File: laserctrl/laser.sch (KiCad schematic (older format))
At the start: 23 parts

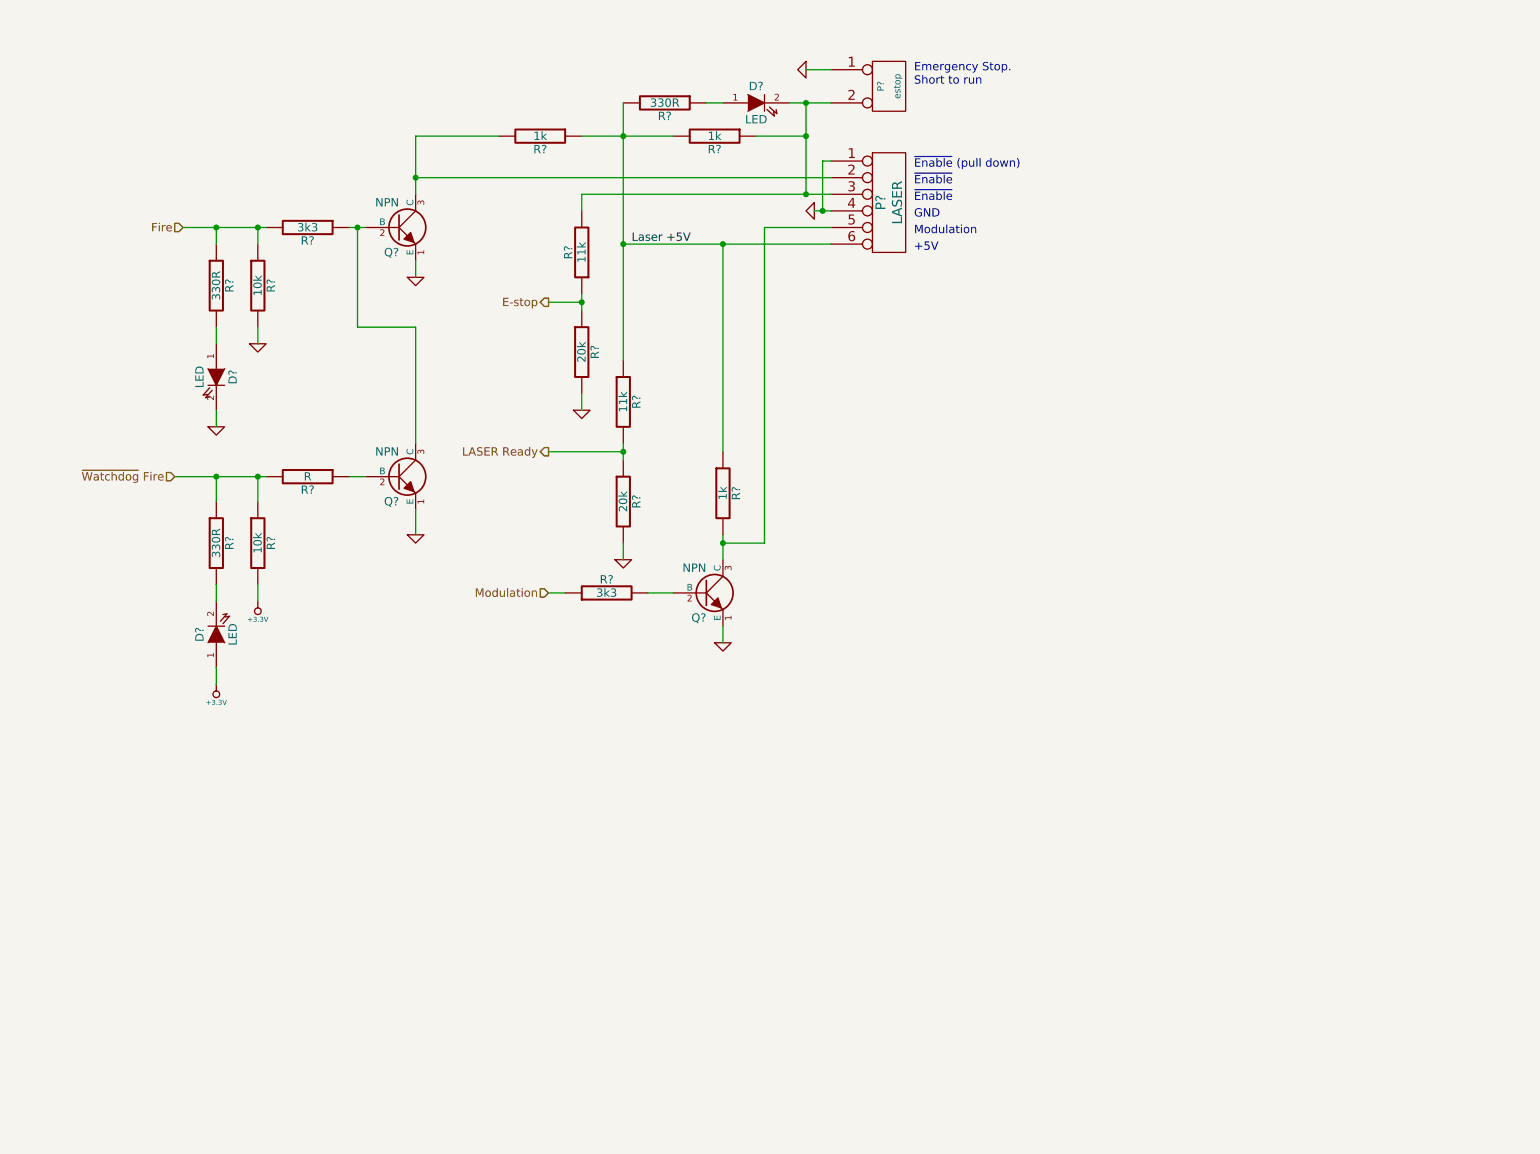
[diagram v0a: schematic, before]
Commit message: Added optocouplers to the LASER interface to protect against induced transients
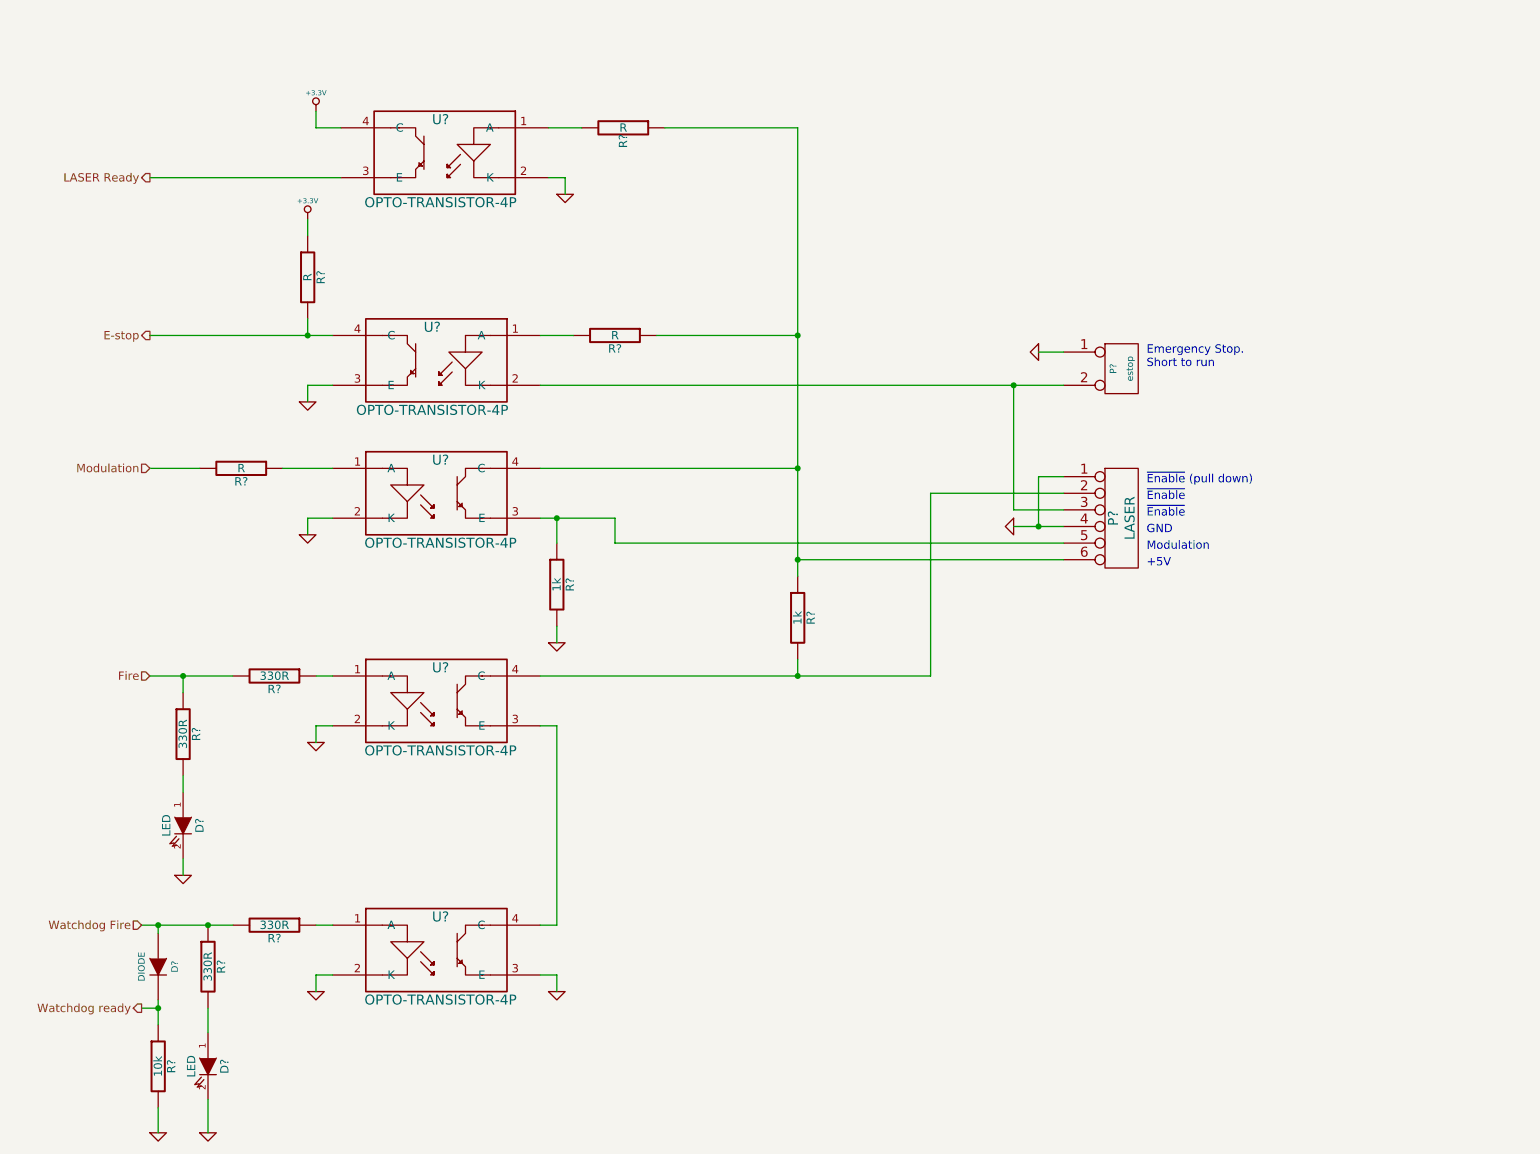
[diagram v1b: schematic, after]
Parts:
- removed D?: LED, symbol LED
- removed Q? (x3): NPN, symbol NPN
- removed R? (x3): 1k, symbol R
- removed R?: 3k3, symbol R
- removed R?: 330R, symbol R
- removed R? (x2): 11k, symbol R
- removed R? (x2): 20k, symbol R
- removed R? (x2): 10k, symbol R
- added D?: DIODE, symbol DIODE
- added R? (x4): R, symbol R
- added R? (x2): 1k, symbol R
- added R?: 10k, symbol R
- added U? (x5): OPTO-TRANSISTOR-4P, symbol OPTO-TRANSISTOR-4P
- R?: value 3k3 -> 330R
- R?: value R -> 330R
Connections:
- net +3.3V: now also R?.1, U?.4 (C); no longer D?.1 (A)
- net E-stop: now also R?.2, U?.4 (C)
- net GND: now also D?.2 (K), R?.2, R?.2, U?.2 (K), U?.2 (K), U?.2 (K), U?.2 (K), U?.3 (E), U?.3 (E)
- net LASER Ready: now also U?.3 (E)
- net Modulation: now also R?.2
- net at P?.2: now also R?.2, U?.4 (C)
- net at P?.2 (PM), P?.3: now also U?.2 (K)
- net at P?.5: now also R?.1, U?.3 (E)
- net at R?.1: now also U?.1 (A) (x2)
- net at R?.2: now also D?.1 (A); no longer D?.2 (K)
- net Laser +5V: no longer names the net of P?.6
- net Laser +5V: now also R?.1, R?.1, R?.1, U?.4 (C)
- net ~Watchdog Fire renamed Watchdog Fire
- net Watchdog Fire: now also D?.1 (A)
- new net: U?.3 (E), U?.4 (C)
- new net: R?.2, U?.1 (A) (x2)
- new net: R?.1, U?.1 (A)
- new net Watchdog ready: D?.2 (K), R?.1
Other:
- moved on the sheet: D?, P?, R?

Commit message: Added transistors to drive the optocouplers
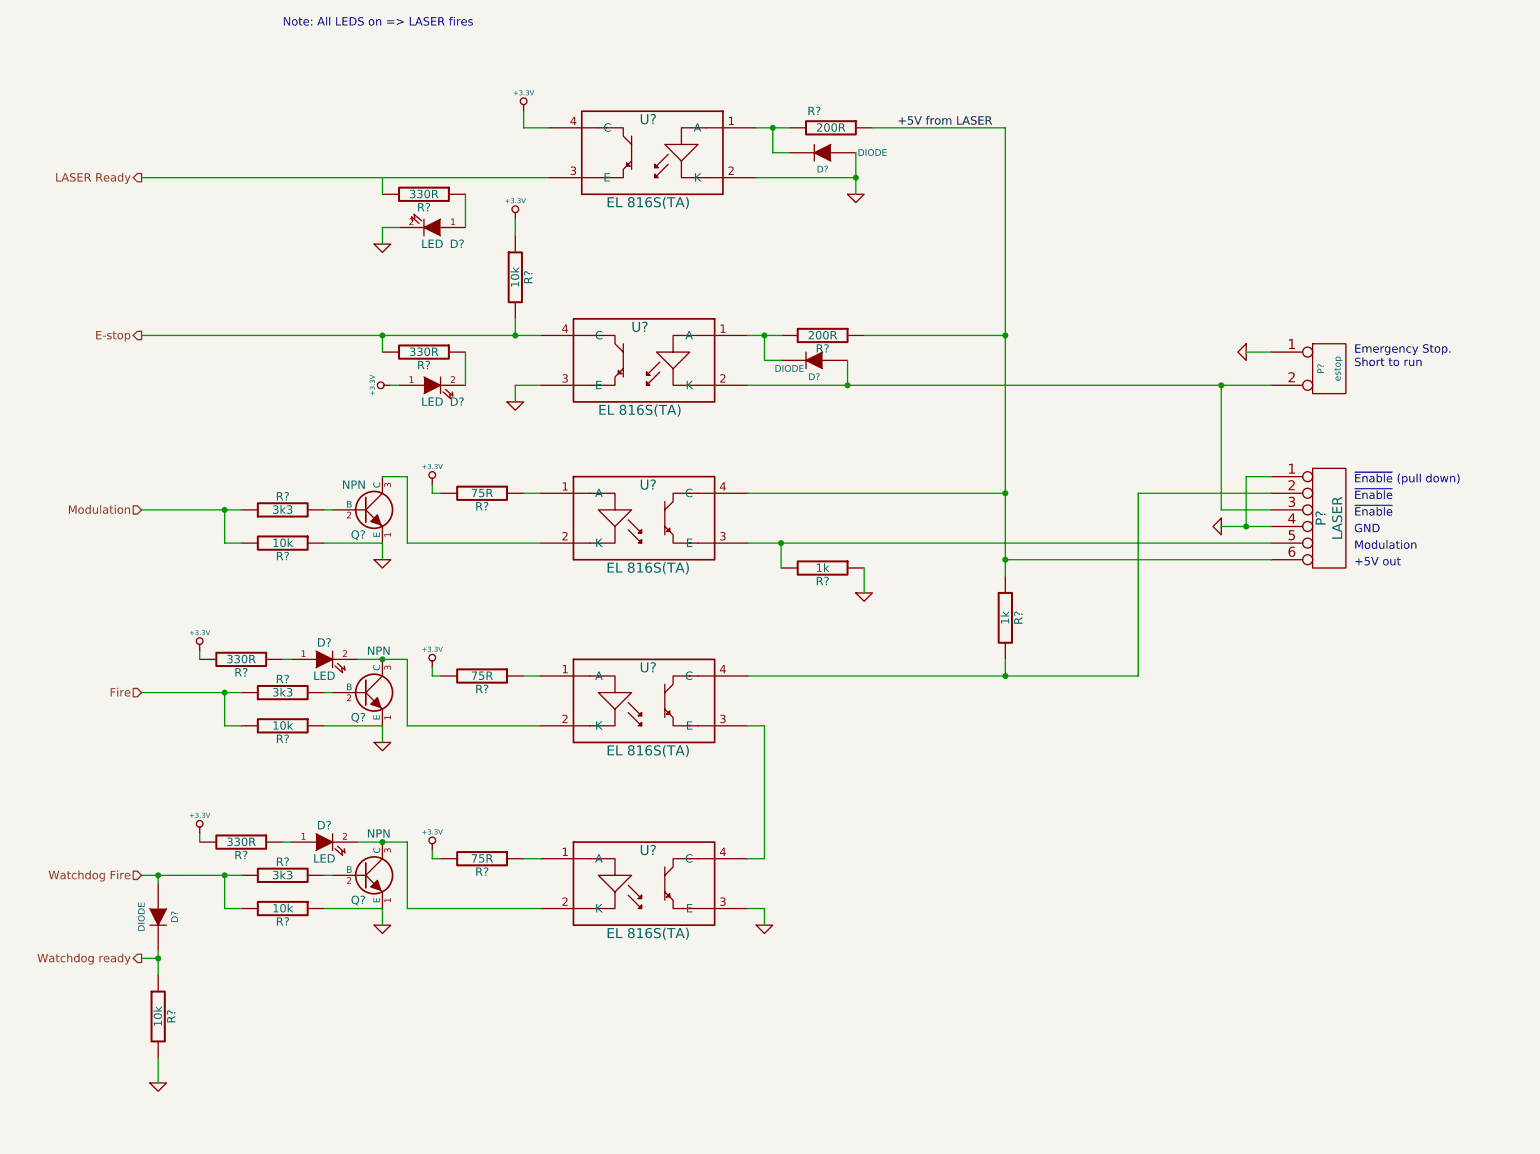
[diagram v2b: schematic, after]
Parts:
- removed D?: LED, symbol LED
- removed R? (x2): 330R, symbol R
- added D? (x3): LED, symbol LED
- added D? (x2): DIODE, symbol DIODE
- added Q? (x3): NPN, symbol NPN
- added R? (x3): 330R, symbol R
- added R? (x3): 10k, symbol R
- added R? (x3): 3k3, symbol R
- added R?: 75R, symbol R
- R?: value 330R -> 75R
- R?: value R -> 10k
- R?: value R -> 75R
- R? (x2): value R -> 200R
- U? (x4): value OPTO-TRANSISTOR-4P -> EL 816S(TA)
- U?: value OPTO-TRANSISTOR-4P -> EL 816S(TA); ELFA (none) -> 75-390-25
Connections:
- net +3.3V: now also R?.2, R?.2, R?.2, D?.1 (A), R?.2, R?.2
- net E-stop: now also R?.2
- net Fire: now also R?.1, R?.2; no longer R?.1, R?.2
- net GND: now also R?.1, D?.1 (A), D?.2 (K), Q?.1 (E), Q?.1 (E), Q?.1 (E), R?.1, R?.1, R?.1; no longer D?.2 (K), R?.2, U?.2 (K), U?.2 (K), U?.2 (K)
- net Modulation: now also R?.1, R?.2; no longer R?.2
- net Watchdog Fire: now also R?.1, R?.2
- net at P?.2 (PM), P?.3, U?.2 (K): now also D?.1 (A)
- net at P?.5, U?.3 (E): now also R?.2; no longer R?.1
- net +5V from LASER: now reaches P?.6, R?.1, R?.1, R?.1, U?.4 (C)
- net at D?.1 (A): now also R?.1; no longer R?.2
- net at U?.1 (A): now also R?.1
- net at R?.2, U?.1 (A): now also D?.2 (K) (x2)
- new net: D?.2 (K), Q?.3 (C), U?.2 (K) (x2)
- new net: Q?.3 (C), U?.2 (K)
- new net: D?.2 (K), R?.1
- new net: D?.1 (A), R?.1 (x2)
- new net: Q?.2 (B), R?.2 (x3)
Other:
- note added: "+5V out"
- note added: "Note: All LEDS on => LASER fires"
- note removed: "+5V"
- moved on the sheet: D?, P?, R?, U?

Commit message: Added a todo list so I don't forget the last bits and tried annotating different ways
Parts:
- gave numbers to parts that had none: 36

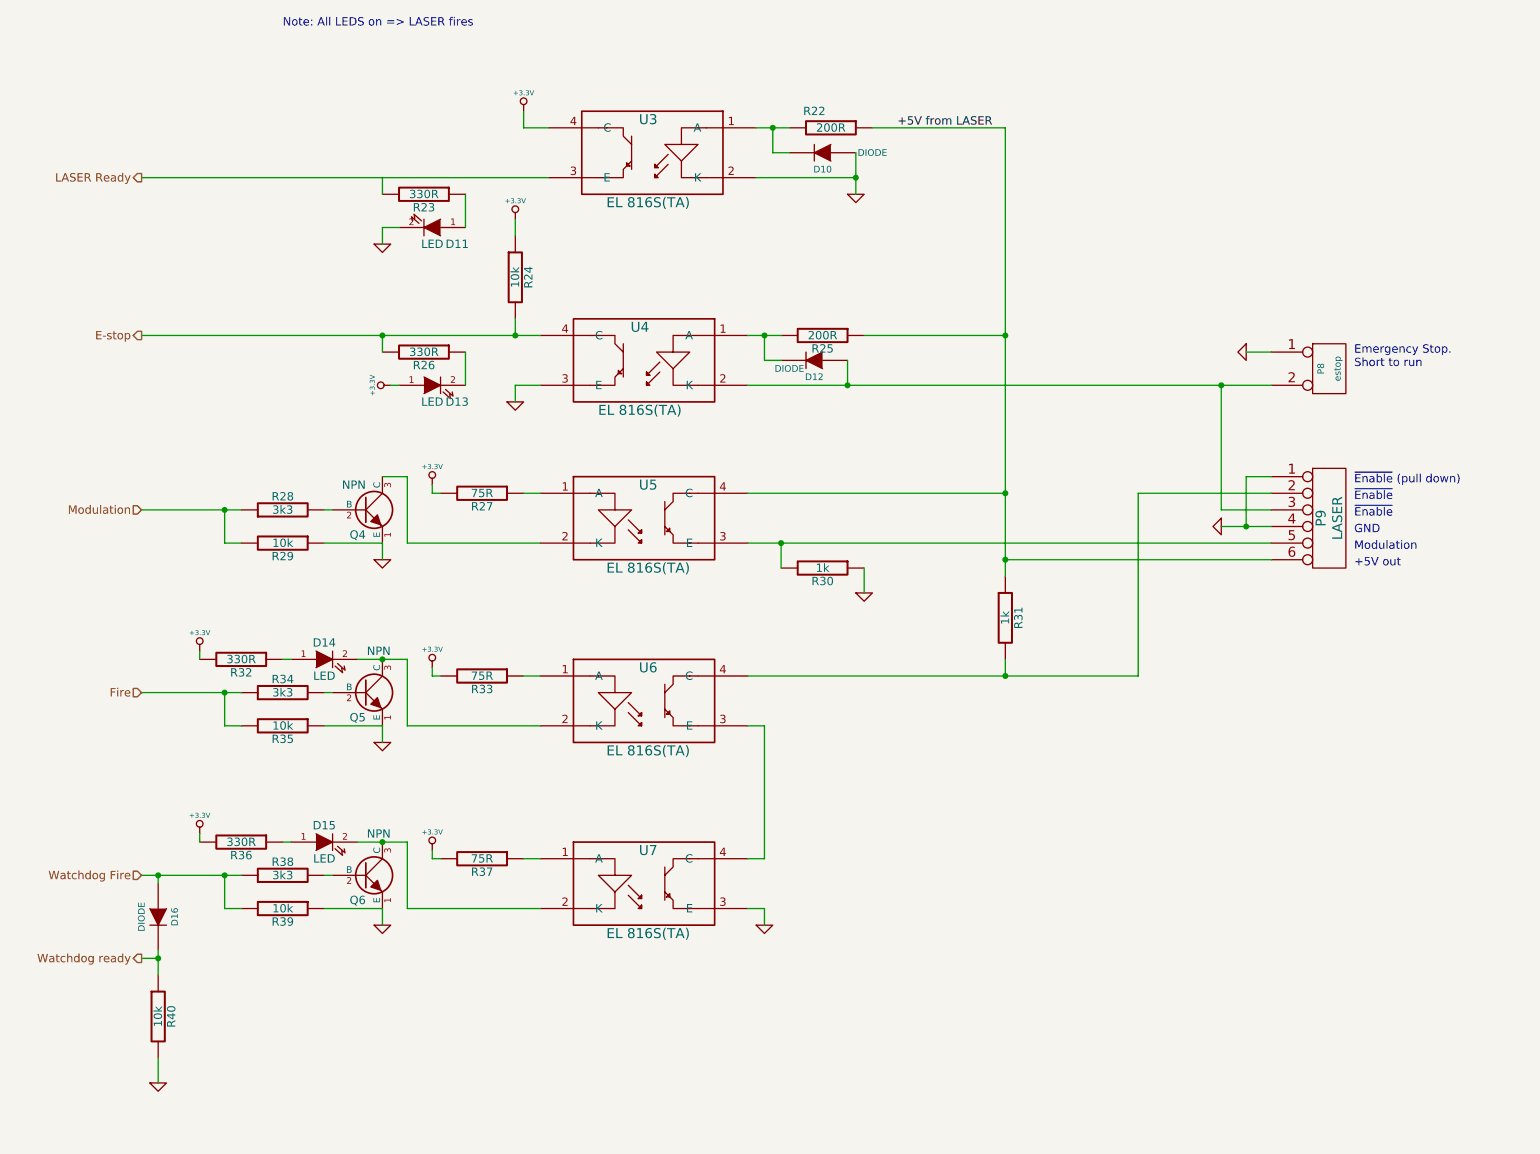
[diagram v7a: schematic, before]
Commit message: Started assigning footprints
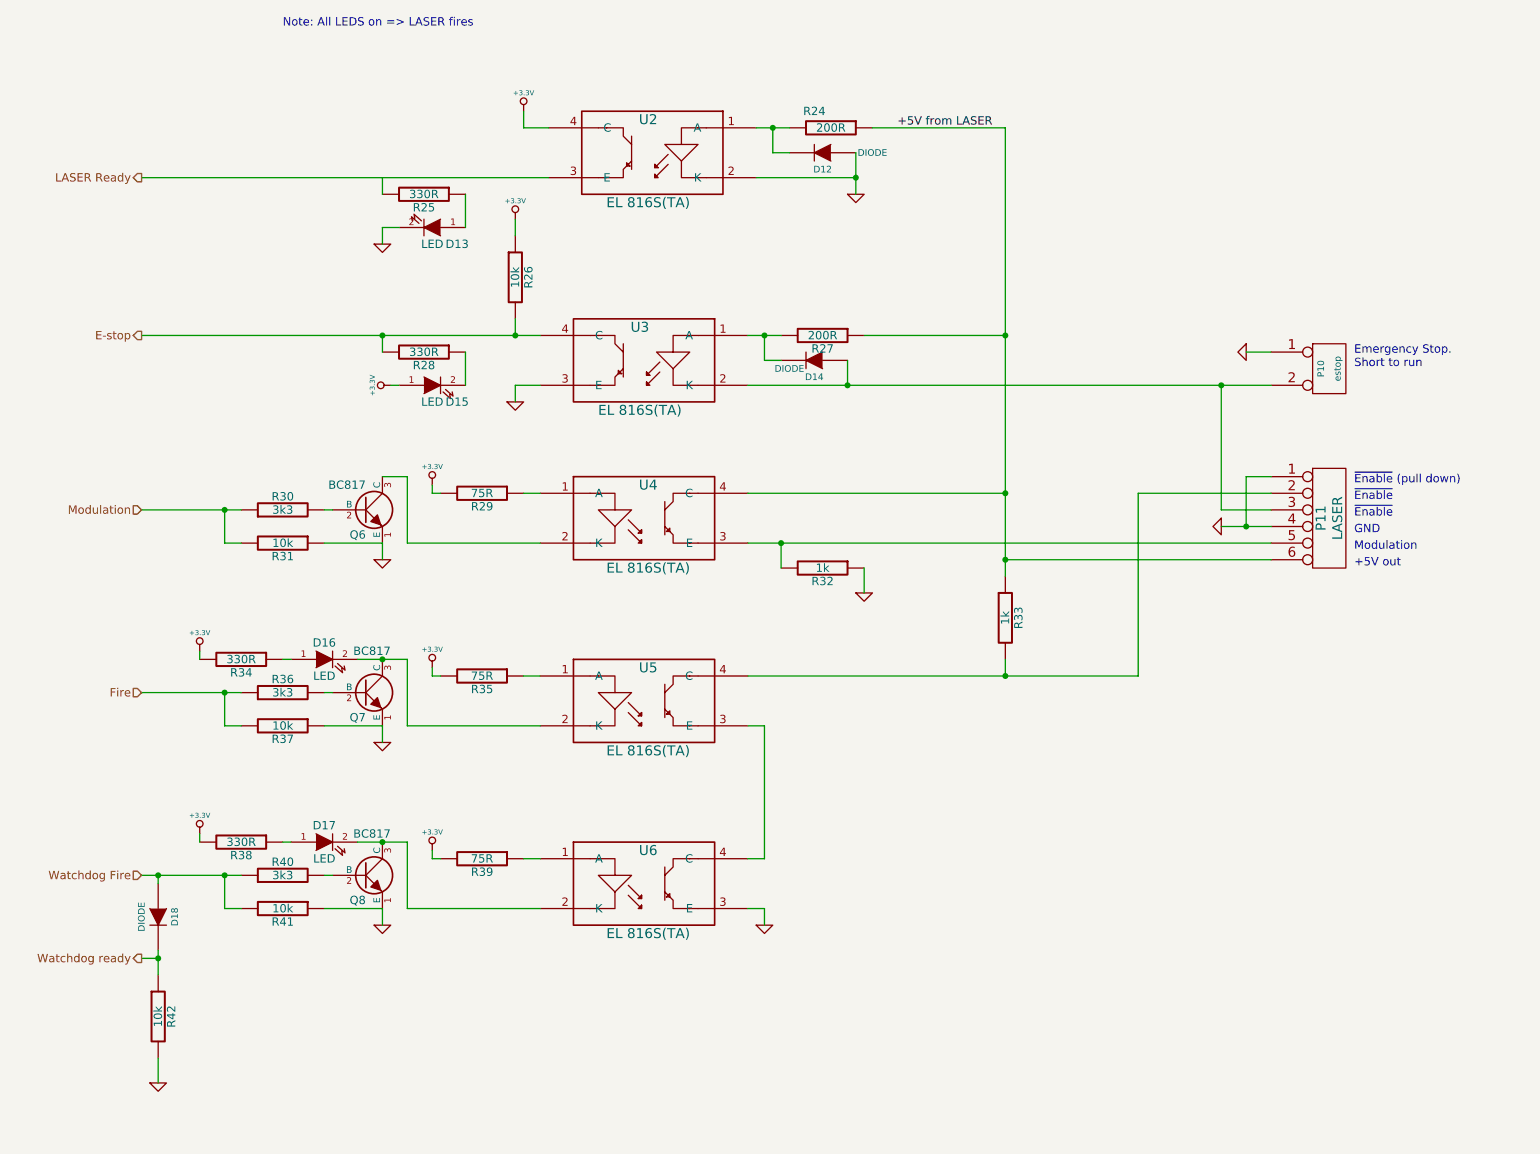
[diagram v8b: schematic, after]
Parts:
- Q6: renamed from Q4; value NPN -> BC817
- Q7: renamed from Q5; value NPN -> BC817
- Q8: renamed from Q6; value NPN -> BC817
- renumbered D10 to D12, D11 to D13, D12 to D14, D13 to D15, D14 to D16, D15 to D17, D16 to D18, P8 to P10, P9 to P11, R22 to R24, R23 to R25, R24 to R26, R25 to R27, R26 to R28, R27 to R29, R28 to R30, R29 to R31, R30 to R32, R31 to R33, R32 to R34, R33 to R35, R34 to R36, R35 to R37, R36 to R38, R37 to R39, R38 to R40, R39 to R41, R40 to R42, U3 to U2, U4 to U3, U5 to U4, U6 to U5, U7 to U6
